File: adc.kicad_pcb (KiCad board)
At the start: 2 copper layers, 53.8 x 69.1 mm, 86 parts, among them J1 Conn_02x08_Odd_Even, J2 Conn_02x08_Odd_Even, J3 Conn_02x08_Odd_Even, J4 Conn_02x08_Odd_Even, J5 Conn_01x04_Male, J9 Conn_02x08_Odd_Even, U1 ADC128D818, U2 ADC128D818, U3 ADC128D818, U4 ADC128D818, U5 ADC128D818

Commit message: i2c lines
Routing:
- net SCL: track 0.00 -> 83.0 mm, vias 0 -> 8
- net SDA: track 0.00 -> 68.0 mm, vias 0 -> 2
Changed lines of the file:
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@@
     (thickness 1.6)
     (drawings 9)
-    (tracks 47)
+    (tracks 122)
     (zones 0)
     (modules 86)
@@
   (gr_line (start 266.192 80.01) (end 266.192 144.78) (layer Edge.Cuts) (width 0.15))
   (gr_line (start 212.344 80.01) (end 266.192 80.01) (layer Edge.Cuts) (width 0.15))
+  (segment (start 263.398 99.064) (end 256.036 106.426) (width 0.2032) (layer B.Cu) (net 35))
+  (segment (start 230.378 106.426) (end 222.78522 106.426) (width 0.2032) (layer B.Cu) (net 35))
+  (via (at 221.488 106.426) (size 0.508) (drill 0.254) (layers F.Cu B.Cu) (net 35))
+  (segment (start 222.78522 106.426) (end 221.488 106.426) (width 0.2032) (layer B.Cu) (net 35))
+  (via (at 221.488 113.284) (size 0.508) (drill 0.254) (layers F.Cu B.Cu) (net 35))
+  (segment (start 221.783 111.096) (end 221.783 112.989) (width 0.2032) (layer B.Cu) (net 35))
+  (segment (start 221.741999 113.030001) (end 221.488 113.284) (width 0.2032) (layer B.Cu) (net 35))
+  (segment (start 221.783 112.989) (end 221.741999 113.030001) (width 0.2032) (layer B.Cu) (net 35))
+  (segment (start 220.726 112.522) (end 221.488 113.284) (width 0.2032) (layer F.Cu) (net 35))
+  (segment (start 221.488 106.426) (end 220.726 107.188) (width 0.2032) (layer F.Cu) (net 35))
+  (segment (start 220.726 107.188) (end 220.726 112.522) (width 0.2032) (layer F.Cu) (net 35))
+  (via (at 233.426 106.426) (size 0.508) (drill 0.254) (layers F.Cu B.Cu) (net 35))
+  (segment (start 233.426 106.426) (end 230.378 106.426) (width 0.2032) (layer B.Cu) (net 35))
+  (segment (start 233.426 106.426) (end 232.918 106.426) (width 0.2032) (layer F.Cu) (net 35))
+  (segment (start 232.918 106.426) (end 232.156 107.188) (width 0.2032) (layer F.Cu) (net 35))
+  (segment (start 232.156 107.188) (end 232.156 112.014) (width 0.2032) (layer F.Cu) (net 35))
+  (via (at 232.664 112.522) (size 0.508) (drill 0.254) (layers F.Cu B.Cu) (net 35))
+  (segment (start 232.156 112.014) (end 232.664 112.522) (width 0.2032) (layer F.Cu) (net 35))
+  (segment (start 233.213 112.227) (end 233.213 111.096) (width 0.2032) (layer B.Cu) (net 35))
+  (segment (start 232.664 112.522) (end 232.918 112.522) (width 0.2032) (layer B.Cu) (net 35))
+  (segment (start 232.918 112.522) (end 233.213 112.227) (width 0.2032) (layer B.Cu) (net 35))
+  (segment (start 256.036 106.426) (end 255.016 106.426) (width 0.2032) (layer B.Cu) (net 35))
+  (segment (start 243.84 106.426) (end 243.586 106.426) (width 0.2032) (layer B.Cu) (net 35))
+  (via (at 243.84 106.426) (size 0.508) (drill 0.254) (layers F.Cu B.Cu) (net 35))
+  (segment (start 243.84 106.426) (end 243.078 107.188) (width 0.2032) (layer F.Cu) (net 35))
+  (segment (start 243.078 107.188) (end 243.078 112.268) (width 0.2032) (layer F.Cu) (net 35))
+  (via (at 243.586 112.522) (size 0.508) (drill 0.254) (layers F.Cu B.Cu) (net 35))
+  (segment (start 243.078 112.268) (end 243.332 112.522) (width 0.2032) (layer F.Cu) (net 35))
+  (segment (start 243.332 112.522) (end 243.586 112.522) (width 0.2032) (layer F.Cu) (net 35))
+  (segment (start 243.586 112.522) (end 243.84 112.522) (width 0.2032) (layer B.Cu) (net 35))
+  (segment (start 244.135 112.227) (end 244.135 111.096) (width 0.2032) (layer B.Cu) (net 35))
+  (segment (start 243.84 112.522) (end 244.135 112.227) (width 0.2032) (layer B.Cu) (net 35))
+  (segment (start 255.016 106.426) (end 243.84 106.426) (width 0.2032) (layer B.Cu) (net 35))
+  (via (at 255.016 106.426) (size 0.508) (drill 0.254) (layers F.Cu B.Cu) (net 35))
+  (segment (start 255.016 106.426) (end 254 107.442) (width 0.2032) (layer F.Cu) (net 35))
+  (segment (start 254 107.442) (end 254 112.268) (width 0.2032) (layer F.Cu) (net 35))
+  (via (at 254.508 112.522) (size 0.508) (drill 0.254) (layers F.Cu B.Cu) (net 35))
+  (segment (start 254 112.268) (end 254.254 112.522) (width 0.2032) (layer F.Cu) (net 35))
+  (segment (start 254.254 112.522) (end 254.508 112.522) (width 0.2032) (layer F.Cu) (net 35))
+  (segment (start 255.057 112.227) (end 255.057 111.096) (width 0.2032) (layer B.Cu) (net 35))
+  (segment (start 254.508 112.522) (end 254.762 112.522) (width 0.2032) (layer B.Cu) (net 35))
+  (segment (start 254.762 112.522) (end 255.057 112.227) (width 0.2032) (layer B.Cu) (net 35))
+  (segment (start 243.586 106.426) (end 240.538 106.426) (width 0.2032) (layer B.Cu) (net 35))
+  (segment (start 239.522 105.6182) (end 239.522 106.426) (width 0.2032) (layer B.Cu) (net 35))
+  (segment (start 239.735 105.4052) (end 239.522 105.6182) (width 0.2032) (layer B.Cu) (net 35))
+  (segment (start 239.735 104.452) (end 239.735 105.4052) (width 0.2032) (layer B.Cu) (net 35))
+  (segment (start 240.538 106.426) (end 239.522 106.426) (width 0.2032) (layer B.Cu) (net 35))
+  (segment (start 239.522 106.426) (end 233.426 106.426) (width 0.2032) (layer B.Cu) (net 35))
+  (segment (start 254.407 110.1428) (end 254.407 111.096) (width 0.2032) (layer B.Cu) (net 36))
+  (segment (start 254.407 109.46363) (end 254.407 110.1428) (width 0.2032) (layer B.Cu) (net 36))
+  (segment (start 263.398 101.604) (end 262.26663 101.604) (width 0.2032) (layer B.Cu) (net 36))
+  (segment (start 262.26663 101.604) (end 256.794 107.07663) (width 0.2032) (layer B.Cu) (net 36))
+  (segment (start 243.95137 107.07663) (end 244.094 107.07663) (width 0.2032) (layer B.Cu) (net 36))
+  (segment (start 243.485 111.096) (end 243.485 107.543) (width 0.2032) (layer B.Cu) (net 36))
+  (segment (start 243.485 107.543) (end 243.95137 107.07663) (width 0.2032) (layer B.Cu) (net 36))
+  (segment (start 232.563 107.43163) (end 232.918 107.07663) (width 0.2032) (layer B.Cu) (net 36))
+  (segment (start 232.563 111.096) (end 232.563 107.43163) (width 0.2032) (layer B.Cu) (net 36))
+  (segment (start 244.094 107.07663) (end 242.316 107.07663) (width 0.2032) (layer B.Cu) (net 36))
+  (segment (start 221.133 110.1428) (end 221.133 111.096) (width 0.2032) (layer B.Cu) (net 36))
+  (segment (start 221.133 107.543) (end 221.133 110.1428) (width 0.2032) (layer B.Cu) (net 36))
+  (segment (start 232.918 107.07663) (end 221.59937 107.07663) (width 0.2032) (layer B.Cu) (net 36))
+  (segment (start 221.59937 107.07663) (end 221.133 107.543) (width 0.2032) (layer B.Cu) (net 36))
+  (segment (start 254.407 107.68563) (end 255.016 107.07663) (width 0.2032) (layer B.Cu) (net 36))
+  (segment (start 254.407 109.46363) (end 254.407 107.68563) (width 0.2032) (layer B.Cu) (net 36))
+  (segment (start 256.794 107.07663) (end 255.016 107.07663) (width 0.2032) (layer B.Cu) (net 36))
+  (segment (start 255.016 107.07663) (end 244.094 107.07663) (width 0.2032) (layer B.Cu) (net 36))
+  (segment (start 242.316 107.07663) (end 232.918 107.07663) (width 0.2032) (layer B.Cu) (net 36))
+  (via (at 242.316 107.07663) (size 0.508) (drill 0.254) (layers F.Cu B.Cu) (net 36))
+  (via (at 240.792 102.87) (size 0.508) (drill 0.254) (layers F.Cu B.Cu) (net 36))
+  (segment (start 240.385 103.277) (end 240.538001 103.123999) (width 0.2032) (layer B.Cu) (net 36))
+  (segment (start 240.385 104.452) (end 240.385 103.277) (width 0.2032) (layer B.Cu) (net 36))
+  (segment (start 240.538001 103.123999) (end 240.792 102.87) (width 0.2032) (layer B.Cu) (net 36))
+  (segment (start 241.3 102.87) (end 240.792 102.87) (width 0.2032) (layer F.Cu) (net 36))
+  (segment (start 242.316 107.07663) (end 242.316 103.886) (width 0.2032) (layer F.Cu) (net 36))
+  (segment (start 242.316 103.886) (end 241.3 102.87) (width 0.2032) (layer F.Cu) (net 36))
   (segment (start 247.65 97.609) (end 247.65 94.742) (width 0.2032) (layer F.Cu) (net 37))
   (segment (start 246.1632 97.282) (end 247.65 95.7952) (width 0.2032) (layer B.Cu) (net 37))

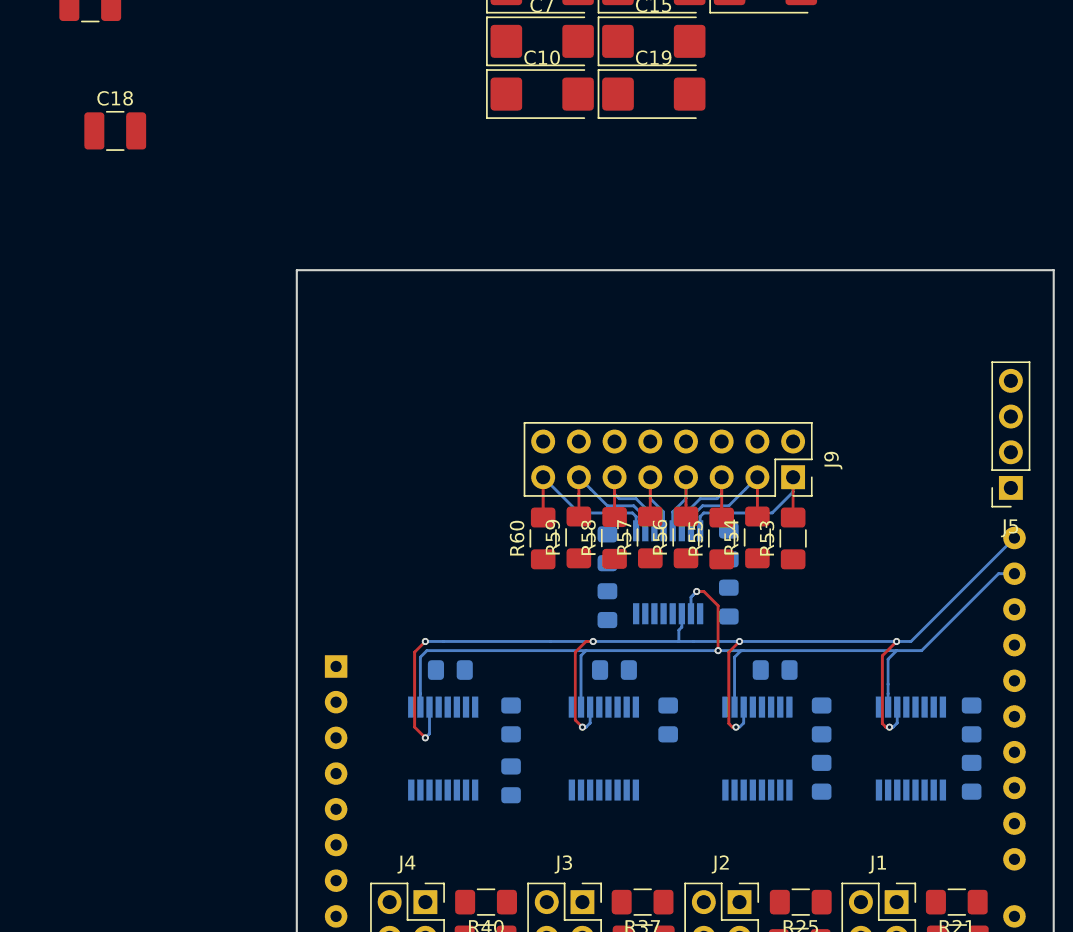
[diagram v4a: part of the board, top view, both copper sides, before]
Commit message: adjust address resitors
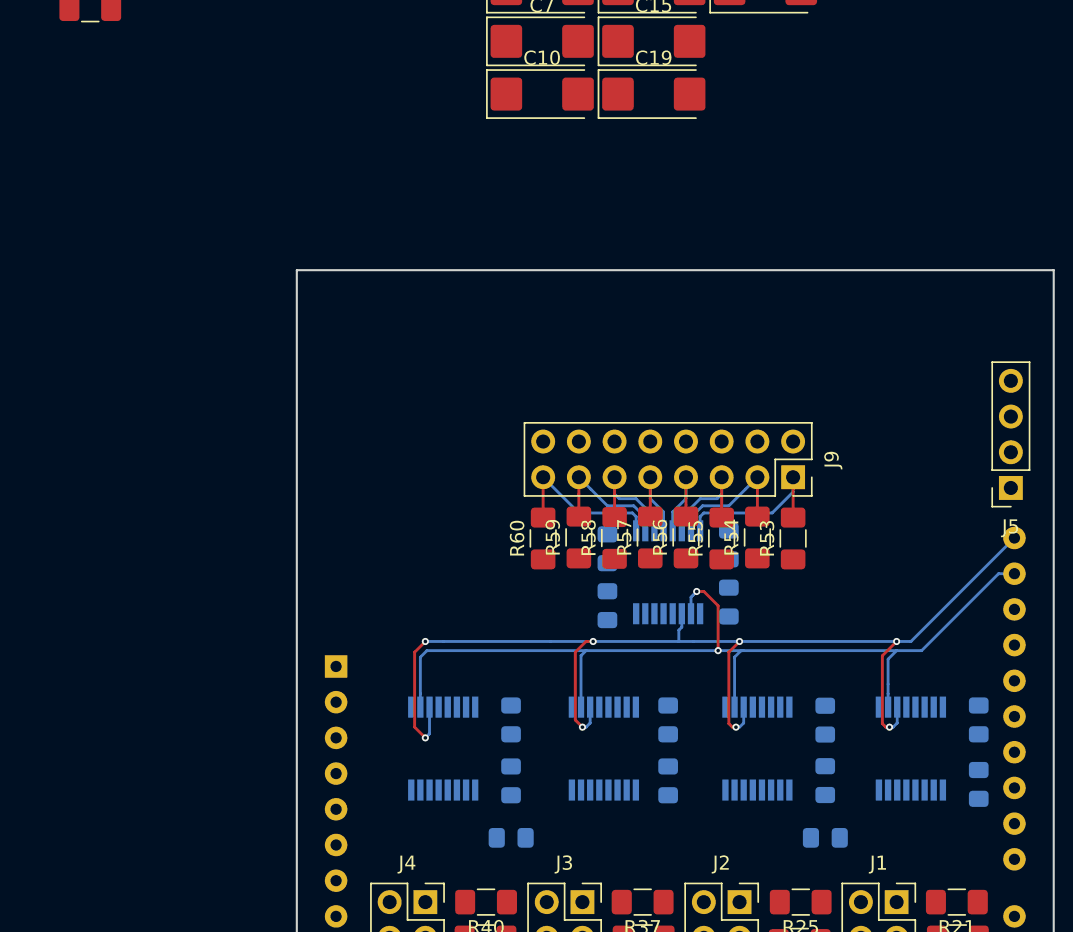
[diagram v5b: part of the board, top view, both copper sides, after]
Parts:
- removed C18: 0.1U CERAMIC, Capacitor_SMD:C_1210_3225Metric_Pad1.42x2.65mm_HandSolder
- moved R9 12.7 mm to (227.6, 120.4), turned to 0 degrees
- moved R3 12.5 mm to (249.9, 120.4), turned to 180 degrees
- moved R7 8.76 mm to (238.8, 116.3), turned to 90 degrees
- moved R2 0.72 mm to (260.9, 116.6), turned to 90 degrees
- moved R1 0.51 mm to (260.9, 112.0), turned to 270 degrees
- moved R5 0.35 mm to (249.9, 116.3)
- moved R4 0.25 mm to (249.9, 112.0), turned to 90 degrees

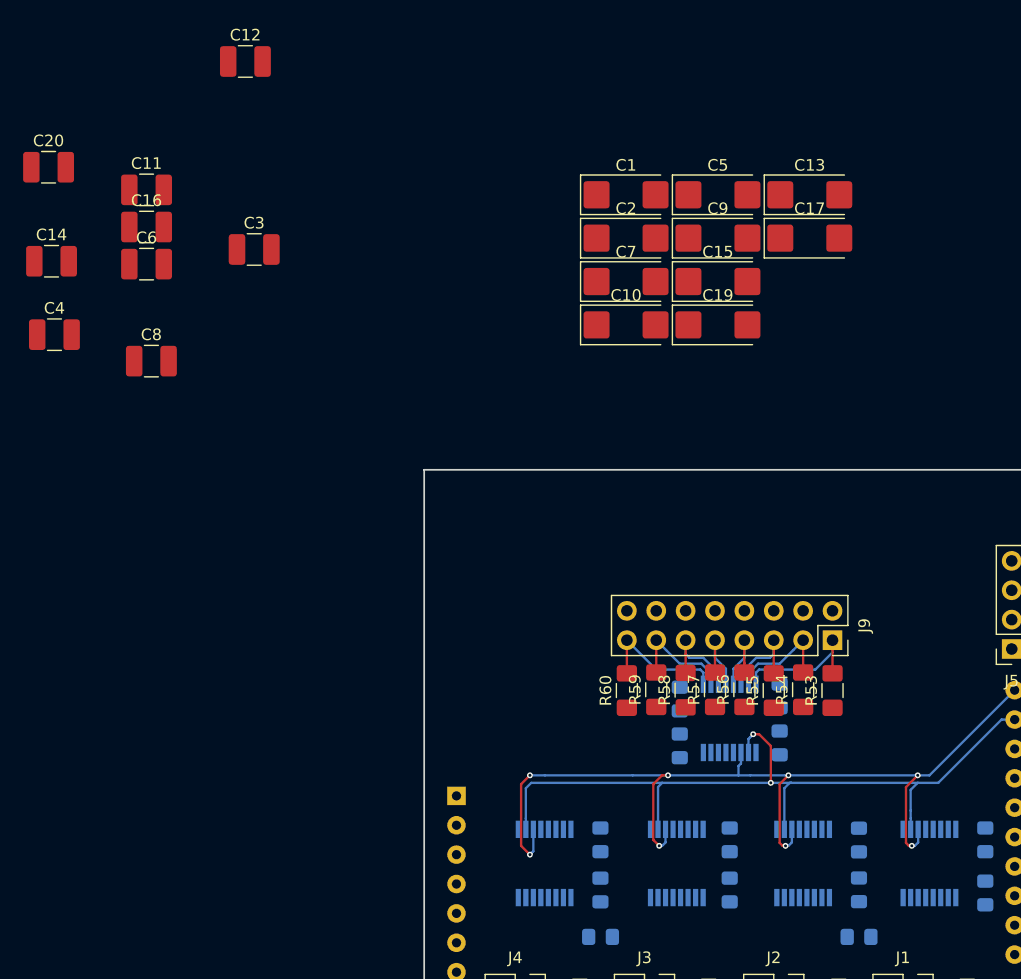
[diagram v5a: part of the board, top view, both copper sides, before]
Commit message: place ceramic caps (switch to 0805?)
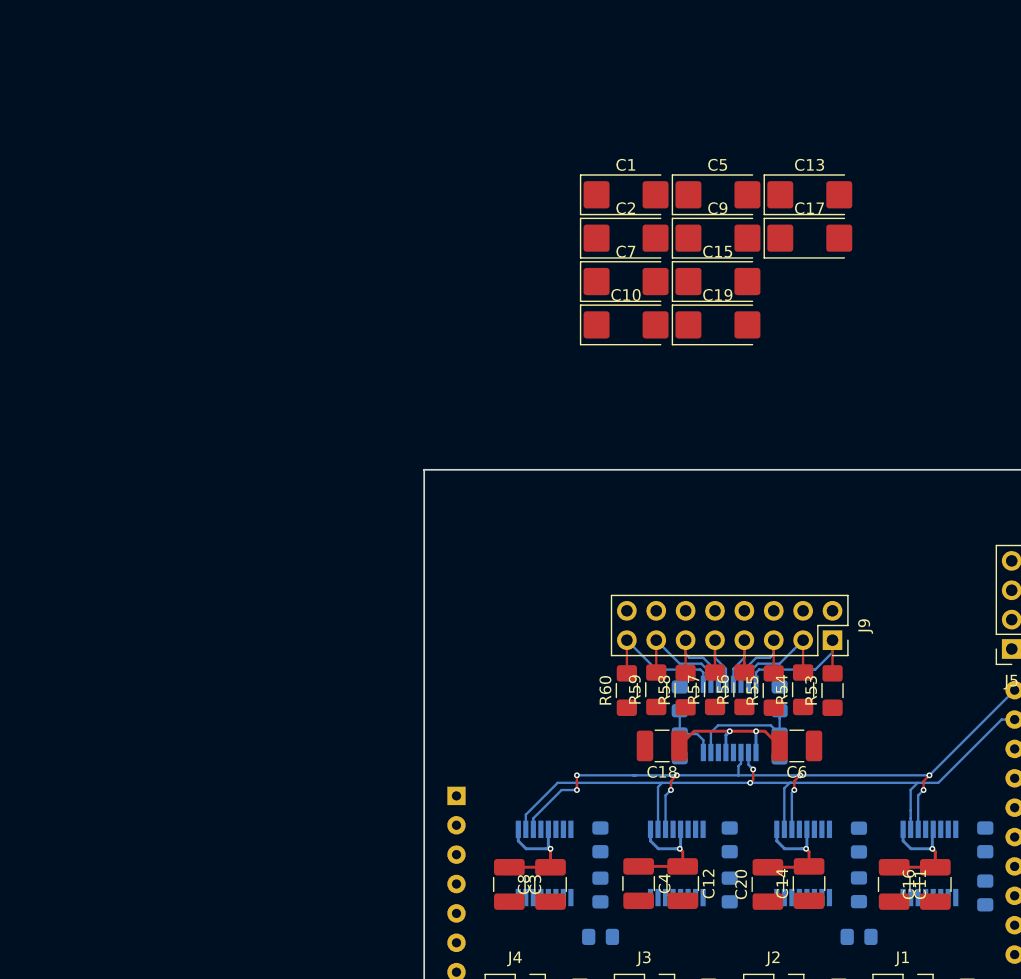
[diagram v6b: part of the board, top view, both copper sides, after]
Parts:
- added C18: 0.1U CERAMIC, Capacitor_SMD:C_1210_3225Metric_Pad1.42x2.65mm_HandSolder, F.Cu at (232.9, 103.9)
- moved C16 88.8 mm to (256.5, 115.9), turned to 90 degrees
- moved C11 88.2 mm to (253.0, 115.9), turned to 270 degrees
- moved C20 87.8 mm to (242.1, 115.9), turned to 90 degrees
- moved C14 84.8 mm to (245.6, 115.8), turned to 90 degrees
- moved C12 80.5 mm to (234.7, 115.8), turned to 270 degrees
- moved C6 70.0 mm to (244.6, 103.9), turned to 180 degrees
- moved C4 69.3 mm to (230.9, 115.8), turned to 270 degrees
- moved C3 59.2 mm to (219.7, 115.9), turned to 270 degrees
- moved C8 56.9 mm to (223.3, 115.9), turned to 90 degrees
- moved R11 9.44 mm to (234.4, 99.8), turned to 90 degrees
- moved R14 8.64 mm to (243.1, 99.8)
- moved R13 4.34 mm to (243.1, 103.9), turned to 270 degrees
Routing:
- net 3V3: track 0.00 -> 57.0 mm, vias 0 -> 6
- net SCL: track 83.0 -> 65.3 mm
- net Net-(R13-Pad1): track 0.00 -> 10.3 mm
- net Net-(R11-Pad1): track 0.00 -> 5.34 mm
- net SDA: track 68.0 -> 62.6 mm

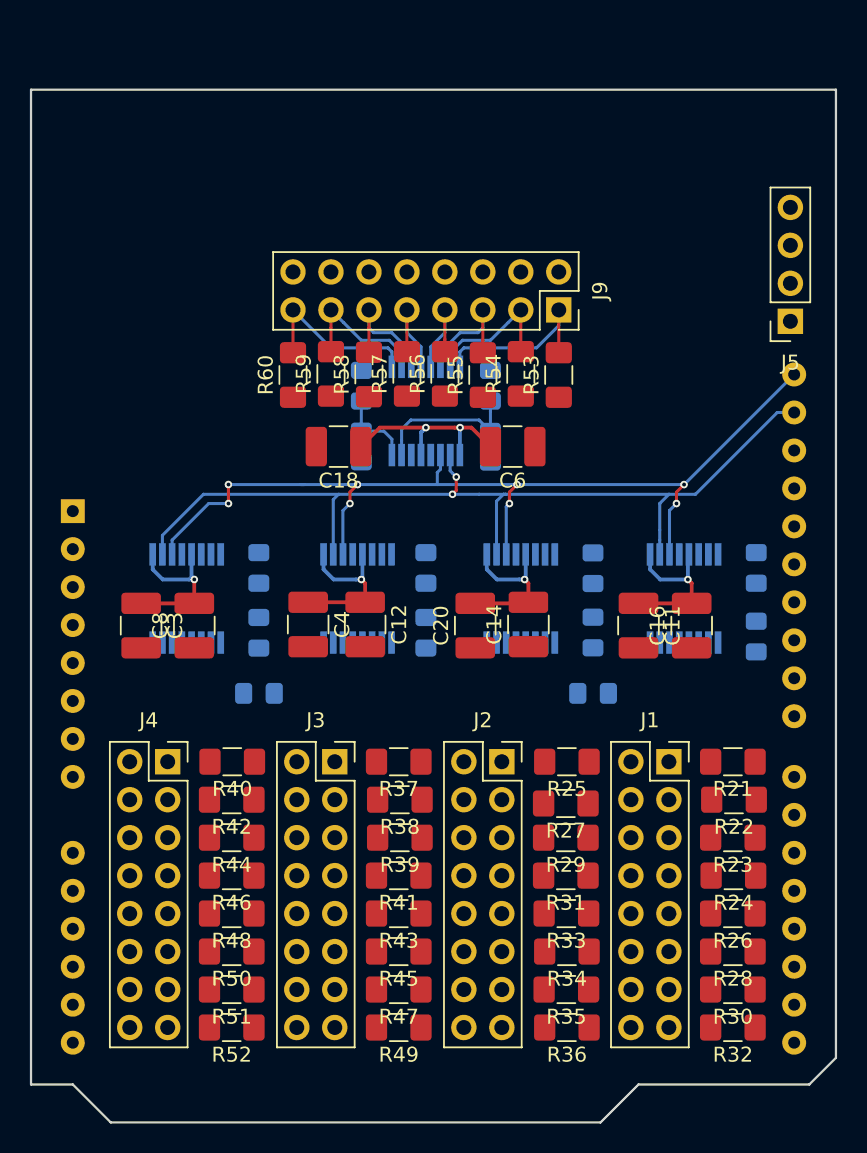
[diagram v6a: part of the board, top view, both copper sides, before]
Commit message: more routing, fill zones
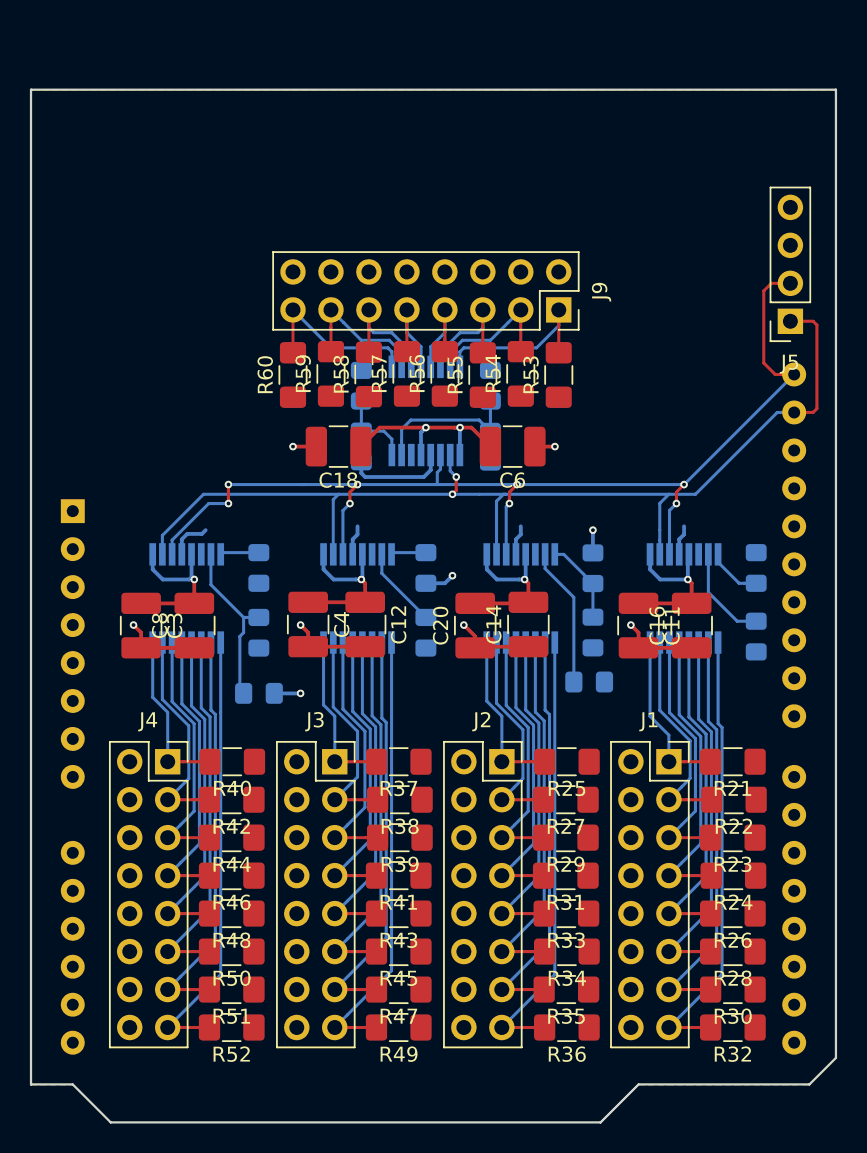
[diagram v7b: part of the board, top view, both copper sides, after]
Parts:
- moved R3 4.07 mm to (249.9, 116.3), turned to 90 degrees
- moved R5 3.32 mm to (249.7, 119.6), turned to 180 degrees
- moved R27 0.25 mm to (248.1, 127.5)
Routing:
- net GND: track 0.00 -> 40.0 mm, vias 0 -> 6
- net Net-(J1-Pad15): track 0.00 -> 30.1 mm
- net Net-(J3-Pad15): track 0.00 -> 30.1 mm
- net Net-(J2-Pad15): track 0.00 -> 30.1 mm
- net Net-(J4-Pad15): track 0.00 -> 30.0 mm
- net Net-(J1-Pad13): track 0.00 -> 27.6 mm
- net Net-(J3-Pad13): track 0.00 -> 27.6 mm
- net Net-(J2-Pad13): track 0.00 -> 27.5 mm
- net Net-(J4-Pad13): track 0.00 -> 27.4 mm
- net Net-(J1-Pad11): track 0.00 -> 25.0 mm
- net Net-(J3-Pad11): track 0.00 -> 25.0 mm
- net Net-(J2-Pad11): track 0.00 -> 25.0 mm
- net Net-(J4-Pad11): track 0.00 -> 24.9 mm
- net Net-(J1-Pad9): track 0.00 -> 22.4 mm
- net Net-(J3-Pad9): track 0.00 -> 22.4 mm
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- added copper zone on F.Cu, net 3V3
- added copper zone on B.Cu, net GND
